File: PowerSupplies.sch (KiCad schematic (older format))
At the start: 46 parts, among them Q301 BC847B-13-F, Q302 BC856B-13-F, Q305 IRFP4321PBF, Q306 IRFP4321PBF, U301 FDA217, U302 LTC7138EMSE-PBF, U303 TPS560200DBVR, U304 TLV70430DBVT, U305 REF2925AIDBZT, U306 TPS560200DBVR

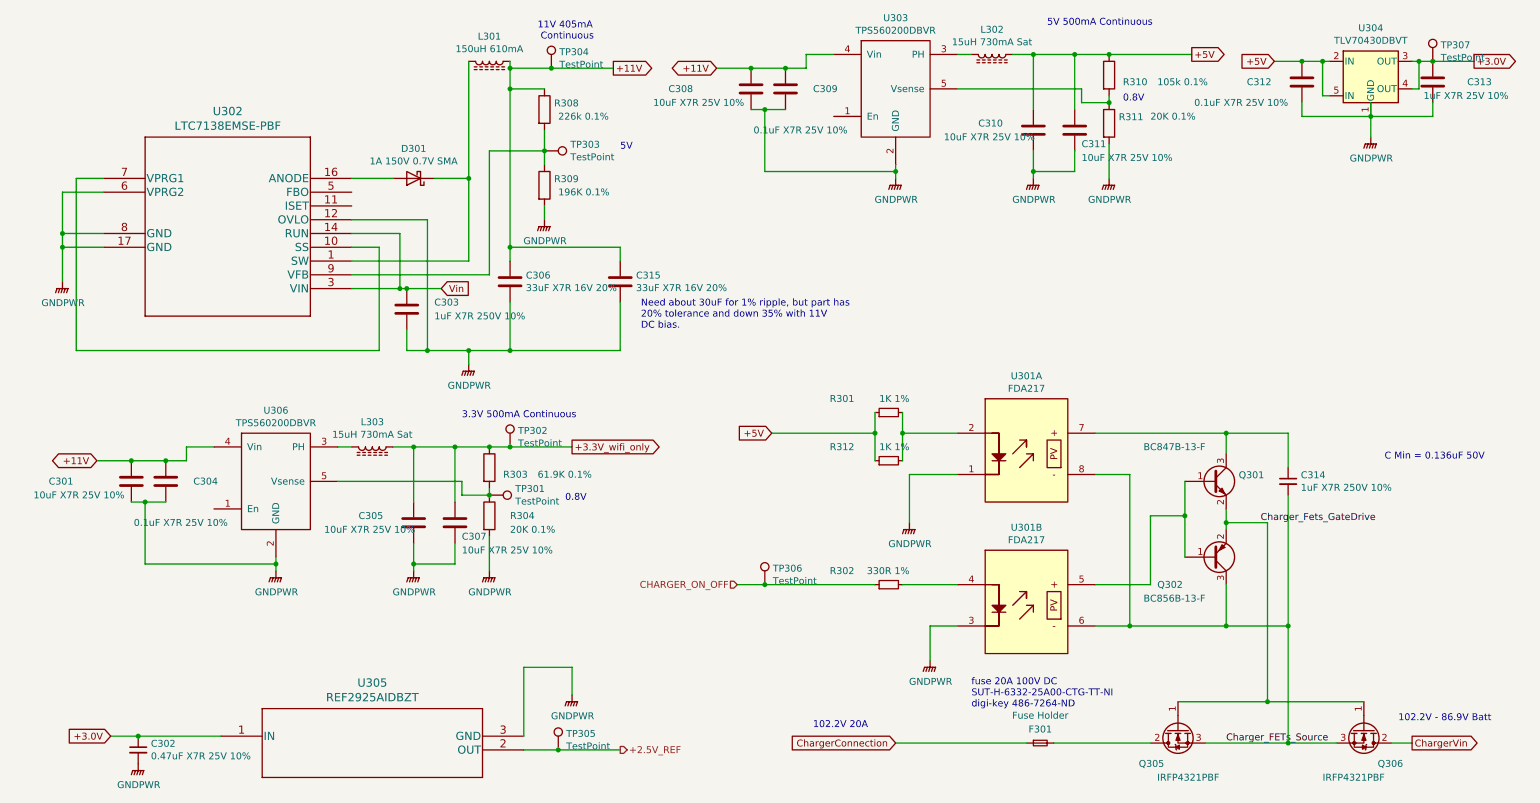
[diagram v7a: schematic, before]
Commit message: Added extra FET in Current sense Auto Ranging circuit to stop the conduction of the body diode of the single FET on the negative half of the mains cycle.  Also change the Values of all the TestPoints from TestPoint to a useful name either the voltage they should read or what they measure, also chaged there layer to front Silks so they can be used.
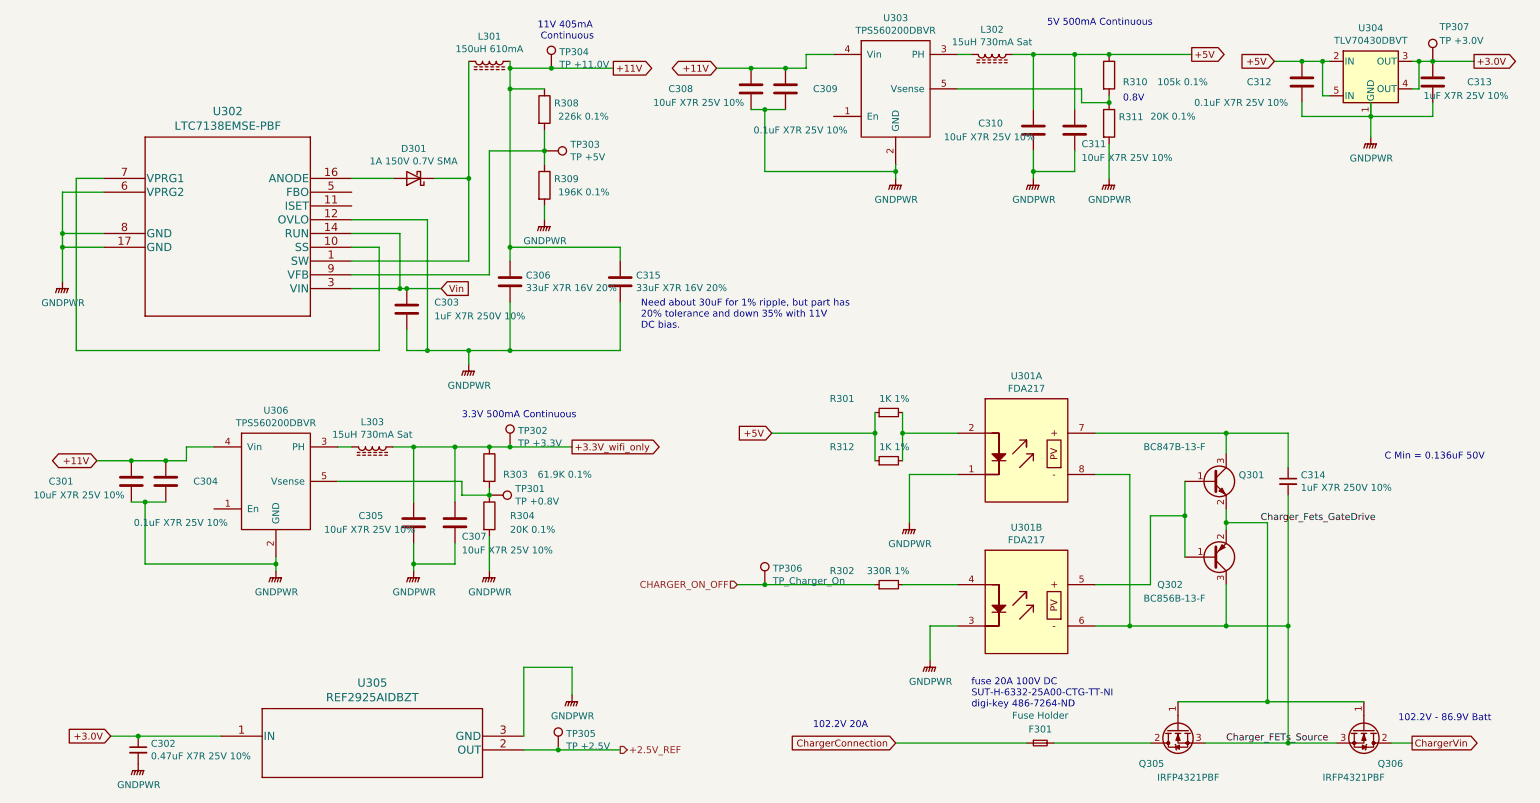
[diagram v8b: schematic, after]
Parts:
- TP301: value TestPoint -> TP +0.8V
- TP302: value TestPoint -> TP +3.3V
- TP303: value TestPoint -> TP +5V
- TP304: value TestPoint -> TP +11.0V
- TP305: value TestPoint -> TP +2.5V
- TP306: value TestPoint -> TP_Charger_On
- TP307: value TestPoint -> TP +3.0V
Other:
- note removed: "5V"
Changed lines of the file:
@@
 P 4250 950
 F 0 "TP304" H 4308 1068 50  0000 L CNN
-F 1 "TestPoint" H 4308 977 50  0000 L CNN
+F 1 "TP +11.0V" H 4308 977 50  0000 L CNN
 F 2 "TestPoint:TestPoint_Pad_3.0x3.0mm" H 4450 950 50  0001 C CNN
 F 3 "~" H 4450 950 50  0001 C CNN
@@
 P 4200 1550
 F 0 "TP303" V 4154 1738 50  0000 L CNN
-F 1 "TestPoint" V 4245 1738 50  0000 L CNN
+F 1 "TP +5V" V 4245 1738 50  0000 L CNN
 F 2 "TestPoint:TestPoint_Pad_3.0x3.0mm" H 4400 1550 50  0001 C CNN
 F 3 "~" H 4400 1550 50  0001 C CNN
@@
 P 3800 4050
 F 0 "TP301" V 3754 4238 50  0000 L CNN
-F 1 "TestPoint" V 3845 4238 50  0000 L CNN
+F 1 "TP +0.8V" V 3845 4238 50  0000 L CNN
 F 2 "TestPoint:TestPoint_Pad_3.0x3.0mm" H 4000 4050 50  0001 C CNN
 F 3 "~" H 4000 4050 50  0001 C CNN
@@
 P 4300 5900
 F 0 "TP305" H 4358 6018 50  0000 L CNN
-F 1 "TestPoint" H 4358 5927 50  0000 L CNN
+F 1 "TP +2.5V" H 4358 5927 50  0000 L CNN
 F 2 "TestPoint:TestPoint_Pad_3.0x3.0mm" H 4500 5900 50  0001 C CNN
 F 3 "~" H 4500 5900 50  0001 C CNN
@@
 U 1 1 6049E6F4
 P 10650 900
-F 0 "TP307" H 10708 1018 50  0000 L CNN
-F 1 "TestPoint" H 10708 927 50  0000 L CNN
+F 0 "TP307" H 10700 1150 50  0000 L CNN
+F 1 "TP +3.0V" H 10700 1050 50  0000 L CNN
 F 2 "TestPoint:TestPoint_Pad_3.0x3.0mm" H 10850 900 50  0001 C CNN
 F 3 "~" H 10850 900 50  0001 C CNN
@@
 P 3950 3700
 F 0 "TP302" H 4008 3818 50  0000 L CNN
-F 1 "TestPoint" H 4008 3727 50  0000 L CNN
+F 1 "TP +3.3V" H 4008 3727 50  0000 L CNN
 F 2 "TestPoint:TestPoint_Pad_3.0x3.0mm" H 4150 3700 50  0001 C CNN
 F 3 "~" H 4150 3700 50  0001 C CNN
@@
 P 5800 4700
 F 0 "TP306" H 5858 4818 50  0000 L CNN
-F 1 "TestPoint" H 5858 4727 50  0000 L CNN
+F 1 "TP_Charger_On" H 5858 4727 50  0000 L CNN
 F 2 "TestPoint:TestPoint_Pad_3.0x3.0mm" H 6000 4700 50  0001 C CNN
 F 3 "~" H 6000 4700 50  0001 C CNN
@@
 Text GLabel 4700 950  2    50   Output ~ 0
 +11V
-Text Notes 4750 1550 0    50   ~ 0
-5V
 Text GLabel 5450 950  0    50   BiDi ~ 0
 +11V
@@
 Text GLabel 950  3800 0    50   BiDi ~ 0
 +11V
-Text Notes 4350 4100 0    50   ~ 0
-0.8V
 Text GLabel 4400 3700 2    50   Output ~ 0
 +3.3V_wifi_only
